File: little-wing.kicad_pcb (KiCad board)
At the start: 2 copper layers, 116.9 x 94.5 mm, 72 parts, among them IC1 AP7335-WG-7, J1 nice!view, J2 Battery, J3 trackball, J4 trackball, SW1 Power, SW2 Reset, U1 nice!nano v2, U2 PMW3610

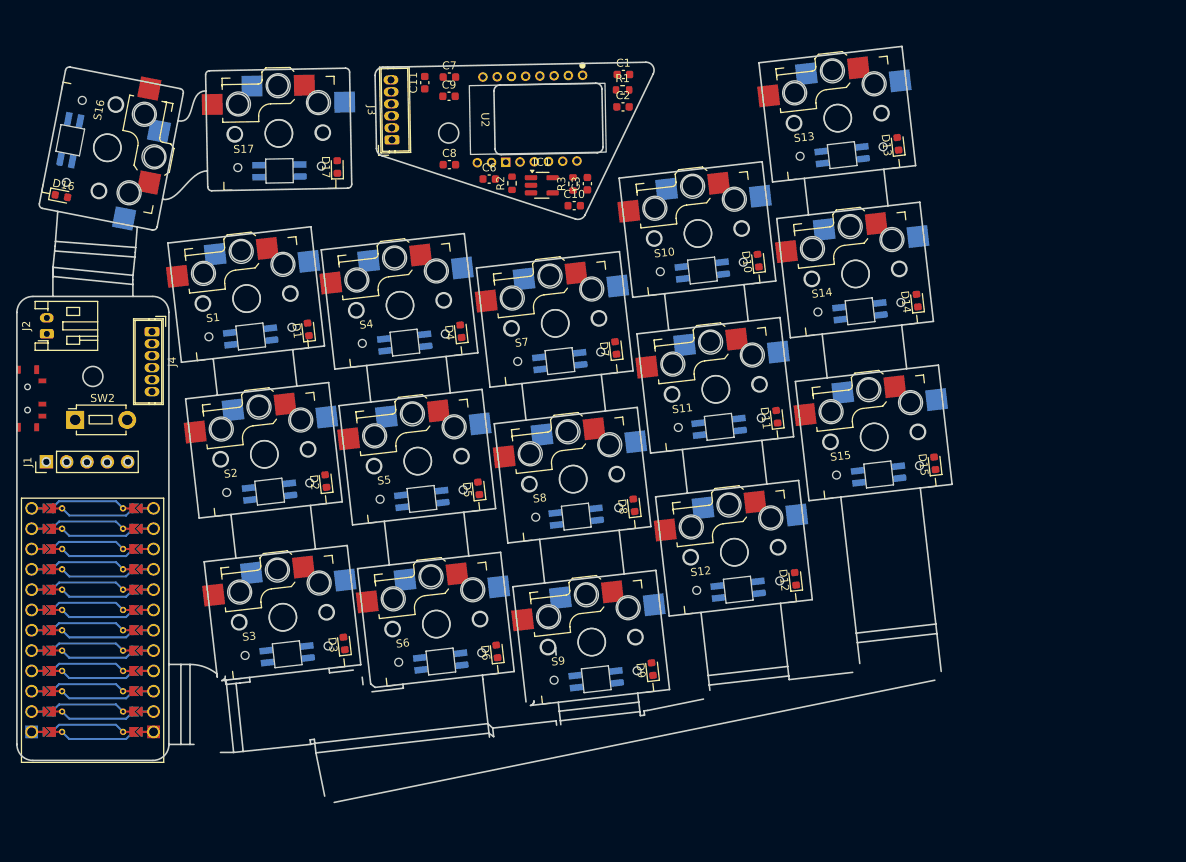
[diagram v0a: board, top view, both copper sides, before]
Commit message: Flipping the components in place
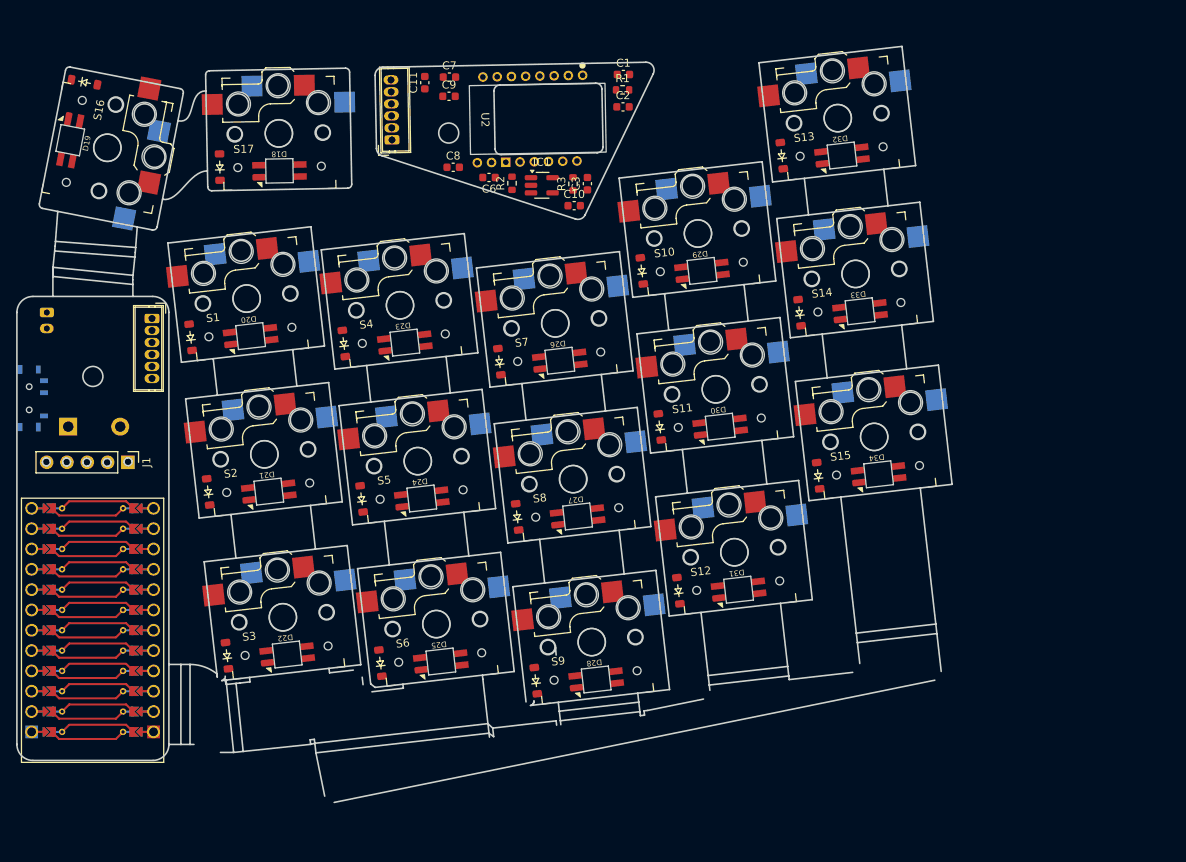
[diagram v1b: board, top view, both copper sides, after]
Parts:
- D1, D10, D11, D12, D13, D14, D15, D16, D17, D2, D3, D4, D5, D6, D7, D8, D9: footprint Diode_SMD:D_0603_1608Metric -> ScottoKeebs_Components:Diode_SOD-123
- D18, D19, D20, D21, D22, D23, D24, D25, D26, D27, D28, D29, D30, D31, D32, D33, D34, J2, SW1, SW2, U1: moved to B.Cu
- moved D14 14.8 mm to (164.7, 85.8)
- moved D2 14.8 mm to (90.8, 108.2)
- moved D1 14.7 mm to (88.6, 88.9)
- moved D3 14.7 mm to (93.2, 128.7)
- moved D4 14.7 mm to (107.8, 89.7)
- moved D12 14.7 mm to (149.6, 120.6)
- moved D5 14.7 mm to (110.0, 109.1)
- moved D11 14.7 mm to (147.2, 100.1)
- moved D17 14.7 mm to (92.2, 67.7)
- moved D8 14.7 mm to (129.4, 111.4)
- moved D15 14.7 mm to (167.1, 106.2)
- moved D7 14.6 mm to (127.2, 92.0)
- moved D6 14.6 mm to (112.3, 129.7)
- moved D9 14.6 mm to (131.8, 131.8)
- moved D10 14.6 mm to (145.0, 80.6)
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
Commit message: Remaking the PCB for better alignment
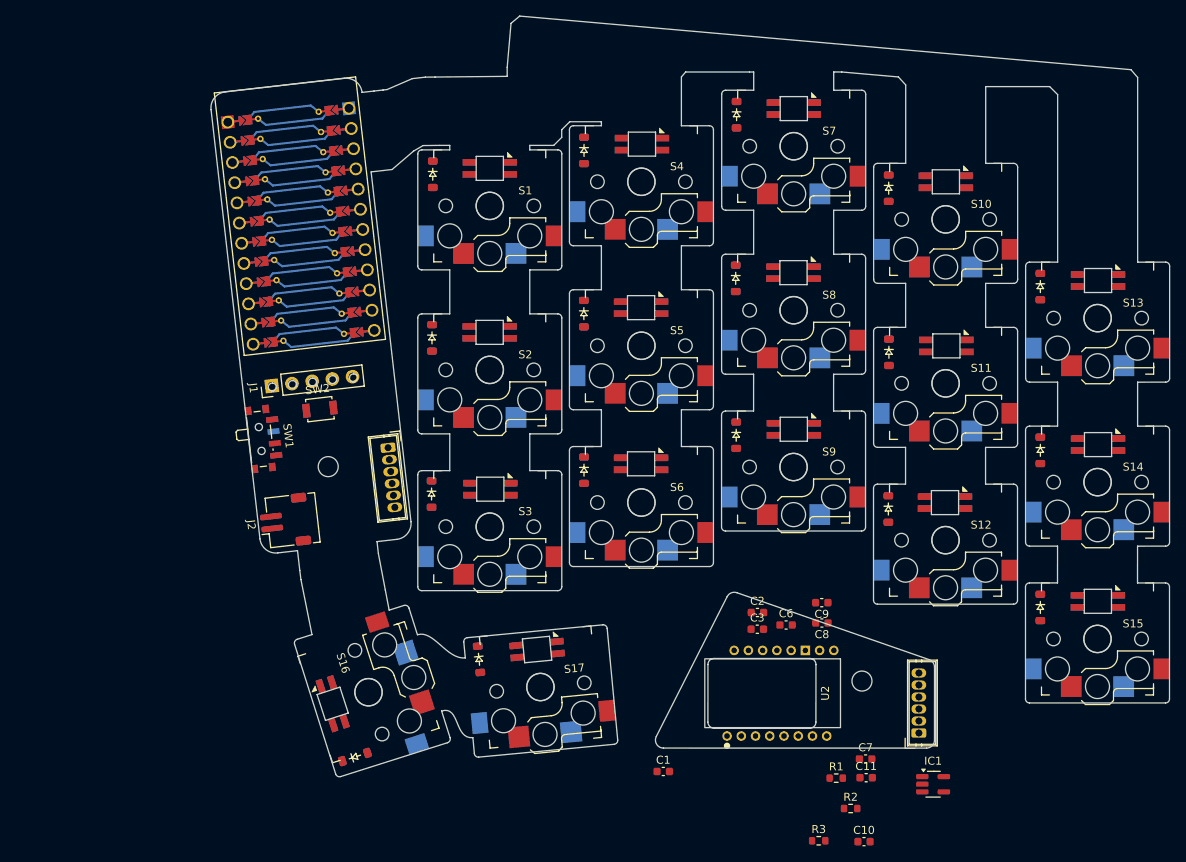
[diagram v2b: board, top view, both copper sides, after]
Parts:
- D1, D10, D11, D12, D13, D14, D15, D16, D17, D2, D3, D4, D5, D6, D7, D8, D9: footprint ScottoKeebs_Components:Diode_SOD-123 -> ScottoKeebs_Components:Diode_SOD-123_Reversible
- D18, D19, D20, D21, D22, D23, D24, D25, D26, D27, D28, D29, D30, D31, D32, D33, D34: footprint ScottoKeebs_Components:LED_SK6812MINI -> ScottoKeebs_Components:LED_SK6812MINI_Reversible; moved to F.Cu
- J2: footprint Connector_JST:JST_PH_S2B-PH-K_1x02_P2.00mm_Horizontal -> Connector_JST:JST_ZH_S2B-ZR-SM4A-TF_1x02-1MP_P1.50mm_Horizontal_Reversible; moved to F.Cu
- S1, S10, S11, S12, S13, S14, S15, S16, S17, S2, S3, S4, S5, S6, S7, S8, S9: footprint keyswitches:Kailh_socket_PG1350_reversible -> keyswitches:Kailh_socket_PG1350_reversible_better
- SW1: footprint switch:switch-MSK-12C02-smd -> Button_Switch_SMD:SW_SPDT_PCM12_Reversible; moved to F.Cu
- SW2: footprint ScottoKeebs_Components:Button_MJTP1243 -> Button_Switch_SMD:SW_SPST_B3U-1000P_Reversible; moved to F.Cu
- U1: moved to F.Cu
- moved D22 111.6 mm to (202.0, 81.8), turned to 0 degrees
- moved D20 111.0 mm to (202.0, 121.9), turned to 0 degrees
- moved D21 103.8 mm to (202.0, 102.3), turned to 0 degrees
- moved C11 102.9 mm to (173.0, 144.0), turned to 0 degrees
- moved C7 99.9 mm to (173.0, 141.6)
- moved J3 99.2 mm to (179.6, 138.4), turned to 90 degrees
- moved D16 90.9 mm to (109.1, 141.4), turned to 18 degrees
- moved R1 90.1 mm to (169.3, 144.0)
- moved IC1 89.4 mm to (181.4, 144.8)
- moved R2 88.9 mm to (171.1, 147.8), turned to 0 degrees
- moved R3 87.7 mm to (167.1, 151.9), turned to 0 degrees
- moved C10 87.4 mm to (172.8, 152.0)
- moved C1 87.3 mm to (147.7, 143.2)
- moved D25 87.1 mm to (183.0, 69.5), turned to 0 degrees
- moved C9 78.6 mm to (167.5, 122.1), turned to 180 degrees
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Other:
- board size 116.9 x 94.5 mm -> 119.8 x 95.1 mm

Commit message: Stashing the work before extending the cutouts
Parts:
- moved D29 0.14 mm to (144.9, 104.9)
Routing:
- net Col 0: track 0.00 -> 74.0 mm, vias 0 -> 3
- net Col 2: track 0.00 -> 73.8 mm, vias 0 -> 3
- net Col 4: track 0.00 -> 73.7 mm, vias 0 -> 3
- net Row 1: track 0.00 -> 73.1 mm, vias 0 -> 6
- net Col 1: track 0.00 -> 73.0 mm, vias 0 -> 3
- net Col 3: track 0.00 -> 73.0 mm, vias 0 -> 3
- net Row 0: track 0.00 -> 28.9 mm, vias 0 -> 6
- net Net-(D16-A): track 0.00 -> 28.5 mm, vias 0 -> 2
- net Net-(D17-A): track 0.00 -> 27.0 mm, vias 0 -> 2
- net Net-(D12-A): track 0.00 -> 26.9 mm, vias 0 -> 2
- net Net-(D13-A): track 0.00 -> 26.8 mm, vias 0 -> 2
- net Net-(D14-A): track 0.00 -> 26.4 mm, vias 0 -> 2
- net Net-(D5-A): track 0.00 -> 26.4 mm, vias 0 -> 2
- net Net-(D11-A): track 0.00 -> 26.4 mm, vias 0 -> 2
- net Net-(D1-A): track 0.00 -> 26.4 mm, vias 0 -> 2
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
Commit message: Making a column work
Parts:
- D1, D10, D11, D12, D13, D14, D15, D16, D17, D2, D3, D4, D5, D6, D7, D8, D9: moved to B.Cu
- moved D20 93.3 mm to (126.0, 67.8)
- moved D33 83.5 mm to (202.0, 102.3)
- moved D22 80.4 mm to (126.0, 107.9)
- moved D21 77.3 mm to (126.0, 88.3)
- moved D32 76.3 mm to (202.0, 81.8)
- moved D34 67.8 mm to (202.0, 121.9)
- moved D23 58.7 mm to (145.0, 64.8)
- moved D31 56.9 mm to (182.9, 109.6)
- moved D29 52.0 mm to (183.0, 69.5)
- moved D25 52.0 mm to (144.9, 104.9)
- moved D30 45.5 mm to (182.9, 90.0)
- moved D28 40.1 mm to (164.1, 100.5)
- moved D26 40.1 mm to (164.0, 60.4)
- moved D24 38.5 mm to (144.9, 85.3)
- moved C2 3.44 mm to (156.0, 123.8), turned to 180 degrees
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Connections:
- D18 pad 1: unconnected-(D18-DOUT-Pad1) -> VCC
- D18 pad 2: GND -> unconnected-(D18-DOUT-Pad2)
- D18 pad 3: Net-(D18-DIN) -> GND
- D18 pad 4: VCC -> Net-(D18-DIN)
- D19 pad 1: Net-(D18-DIN) -> VCC
- D19 pad 2: GND -> Net-(D18-DIN)
- D19 pad 3: Net-(D19-DIN) -> GND
- D19 pad 4: VCC -> Net-(D19-DIN)
- D20 pad 1: Net-(D19-DIN) -> VCC
- D20 pad 2: GND -> Net-(D19-DIN)
- D20 pad 3: Net-(D20-DIN) -> GND
- D20 pad 4: VCC -> Net-(D20-DIN)
- D21 pad 1: Net-(D20-DIN) -> VCC
- D21 pad 2: GND -> Net-(D20-DIN)
- D21 pad 3: Net-(D21-DIN) -> GND
- D21 pad 4: VCC -> Net-(D21-DIN)
- D22 pad 1: Net-(D21-DIN) -> VCC
- D22 pad 2: GND -> Net-(D21-DIN)
- D22 pad 3: Net-(D22-DIN) -> GND
- D22 pad 4: VCC -> Net-(D22-VDD)
- D23 pad 1: Net-(D22-DIN) -> VCC
- D23 pad 2: GND -> Net-(D22-VDD)
- D23 pad 3: Net-(D23-DIN) -> GND
- D23 pad 4: VCC -> Net-(D23-DIN)
- D24 pad 1: Net-(D23-DIN) -> VCC
- D24 pad 2: GND -> Net-(D23-DIN)
- D24 pad 3: Net-(D24-DIN) -> GND
- D24 pad 4: VCC -> Net-(D24-DIN)
- D25 pad 1: Net-(D24-DIN) -> VCC
- D25 pad 2: GND -> Net-(D24-DIN)
- D25 pad 3: Net-(D25-DIN) -> GND
- D25 pad 4: VCC -> Net-(D25-DIN)
- D26 pad 1: Net-(D25-DIN) -> VCC
- D26 pad 2: GND -> Net-(D25-DIN)
- D26 pad 3: Net-(D26-DIN) -> GND
- D26 pad 4: VCC -> Net-(D26-DIN)
- D27 pad 1: Net-(D26-DIN) -> VCC
- D27 pad 2: GND -> Net-(D26-DIN)
- D27 pad 3: Net-(D27-DIN) -> GND
- D27 pad 4: VCC -> Net-(D27-DIN)
- D28 pad 1: Net-(D27-DIN) -> VCC
- D28 pad 2: GND -> Net-(D27-DIN)
- D28 pad 3: Net-(D28-DIN) -> GND
- D28 pad 4: VCC -> Net-(D28-VDD)
- D29 pad 1: Net-(D28-DIN) -> VCC
- D29 pad 2: GND -> Net-(D28-VDD)
- D29 pad 3: Net-(D29-DIN) -> GND
- D29 pad 4: VCC -> Net-(D29-DIN)
- D30 pad 1: Net-(D29-DIN) -> VCC
- D30 pad 2: GND -> Net-(D29-DIN)
- D30 pad 3: Net-(D30-DIN) -> GND
- D30 pad 4: VCC -> Net-(D30-DIN)
- D31 pad 1: Net-(D30-DIN) -> VCC
- D31 pad 2: GND -> Net-(D30-DIN)
- D31 pad 3: Net-(D31-DIN) -> GND
- D31 pad 4: VCC -> Net-(D31-DIN)
- D32 pad 1: Net-(D31-DIN) -> VCC
- D32 pad 2: GND -> Net-(D31-DIN)
- D32 pad 3: Net-(D32-DIN) -> GND
- D32 pad 4: VCC -> Net-(D32-DIN)
- D33 pad 1: Net-(D32-DIN) -> VCC
- D33 pad 2: GND -> Net-(D32-DIN)
- D33 pad 3: Net-(D33-DIN) -> GND
- D33 pad 4: VCC -> Net-(D33-VDD)
- D34 pad 1: Net-(D33-DIN) -> VCC
- D34 pad 2: GND -> Net-(D33-VDD)
- D34 pad 3: RGB -> GND
- D34 pad 4: VCC -> RGB
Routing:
- net GND: track 0.00 -> 291.4 mm, vias 0 -> 15
- net VCC: track 0.00 -> 276.9 mm, vias 0 -> 17
- net Row 2: track 13.5 -> 194.6 mm, vias 5 -> 8
- net RGB: track 0.00 -> 82.6 mm, vias 0 -> 1
- net Net-(D32-DIN): track 0.00 -> 74.3 mm, vias 0 -> 2
- net Net-(D25-DIN): track 0.00 -> 70.7 mm, vias 0 -> 2
- net Net-(D22-VDD): track 0.00 -> 69.3 mm, vias 0 -> 2
- net Col 4: track 73.7 -> 124.4 mm
- net Row 1: track 73.1 -> 123.7 mm
- net Net-(D31-DIN): track 0.00 -> 46.9 mm, vias 0 -> 2
- net Net-(D23-DIN): track 0.00 -> 45.7 mm, vias 0 -> 2
- net Net-(D20-DIN): track 0.00 -> 45.4 mm, vias 0 -> 2
- net Net-(D24-DIN): track 0.00 -> 45.3 mm, vias 0 -> 2
- net Net-(D21-DIN): track 0.00 -> 44.7 mm, vias 0 -> 2
- net Net-(D33-VDD): track 0.00 -> 42.5 mm, vias 0 -> 2
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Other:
- outline, holes or cut-outs redrawn

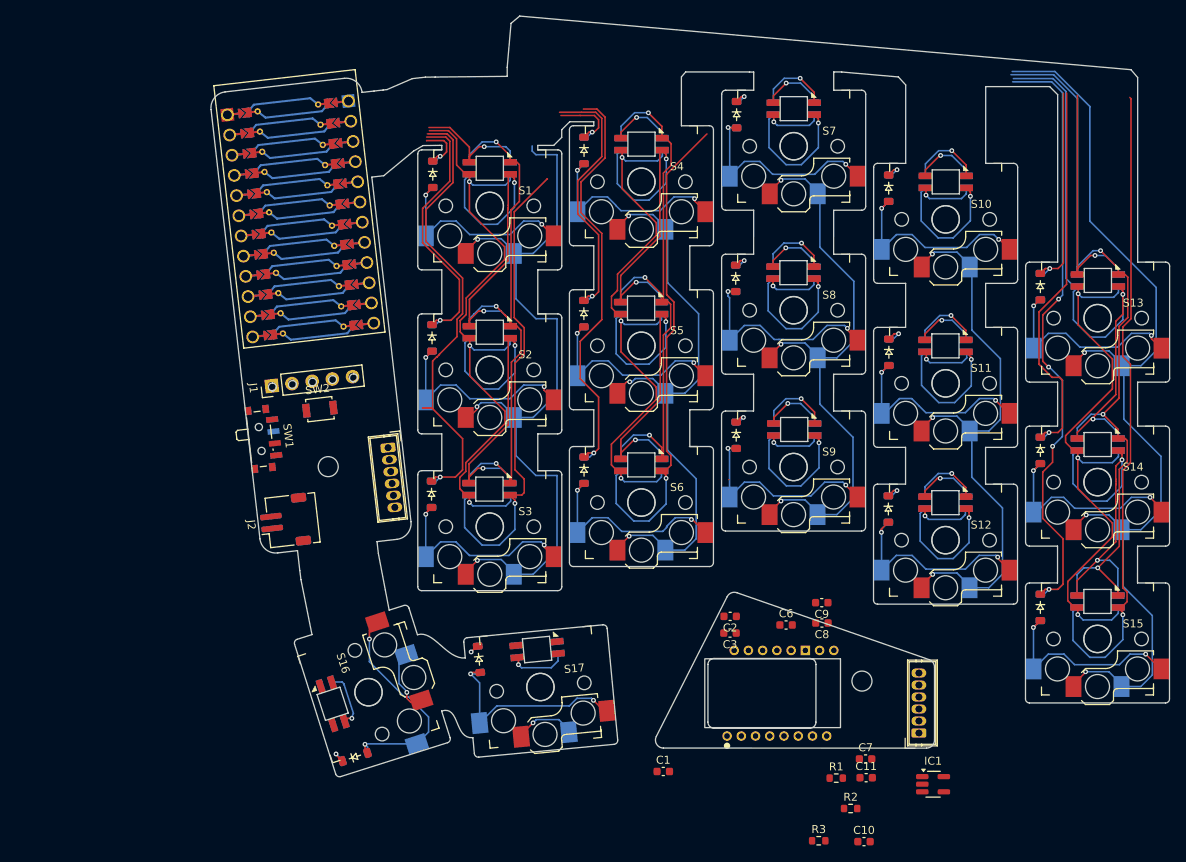
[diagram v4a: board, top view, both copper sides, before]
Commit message: Sorting out the main reversible pads
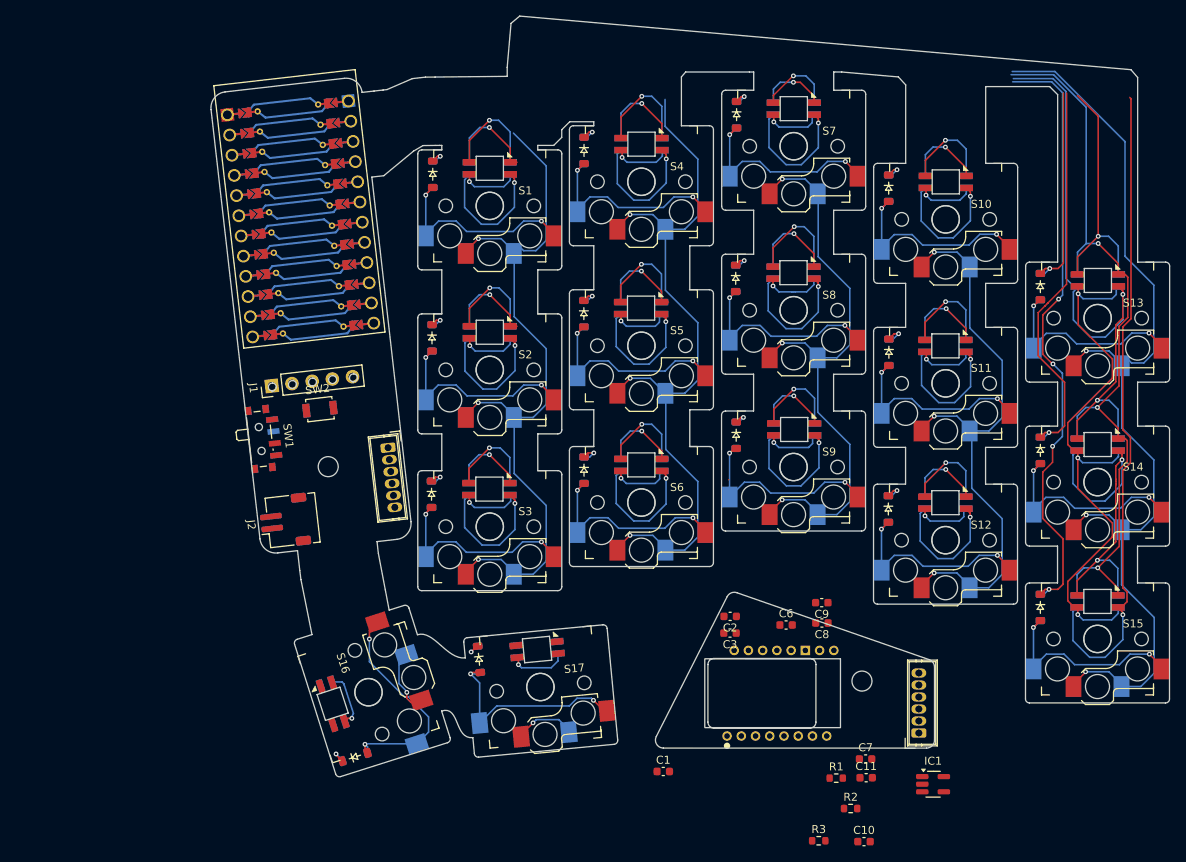
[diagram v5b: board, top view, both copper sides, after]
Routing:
- net Row 2: track 194.6 -> 87.9 mm
- net VCC: track 276.9 -> 175.8 mm
- net GND: track 291.4 -> 226.6 mm
- net Row 1: track 123.7 -> 62.4 mm
- net Net-(D25-DIN): track 70.7 -> 26.9 mm
- net Net-(D22-VDD): track 69.3 -> 30.2 mm
- net Col 1: track 73.0 -> 94.2 mm
- net Net-(D24-DIN): track 45.3 -> 28.4 mm
- net Net-(D23-DIN): track 45.7 -> 29.3 mm
- net Net-(D20-DIN): track 45.4 -> 29.4 mm
- net Net-(D21-DIN): track 44.7 -> 28.8 mm
- net Row 0: track 50.2 -> 39.0 mm
- net Net-(D26-DIN): track 24.5 -> 29.5 mm
- net Col 0: track 98.6 -> 93.7 mm
- net Net-(D29-DIN): track 24.6 -> 29.1 mm
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
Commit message: Connecting the reversible pads together
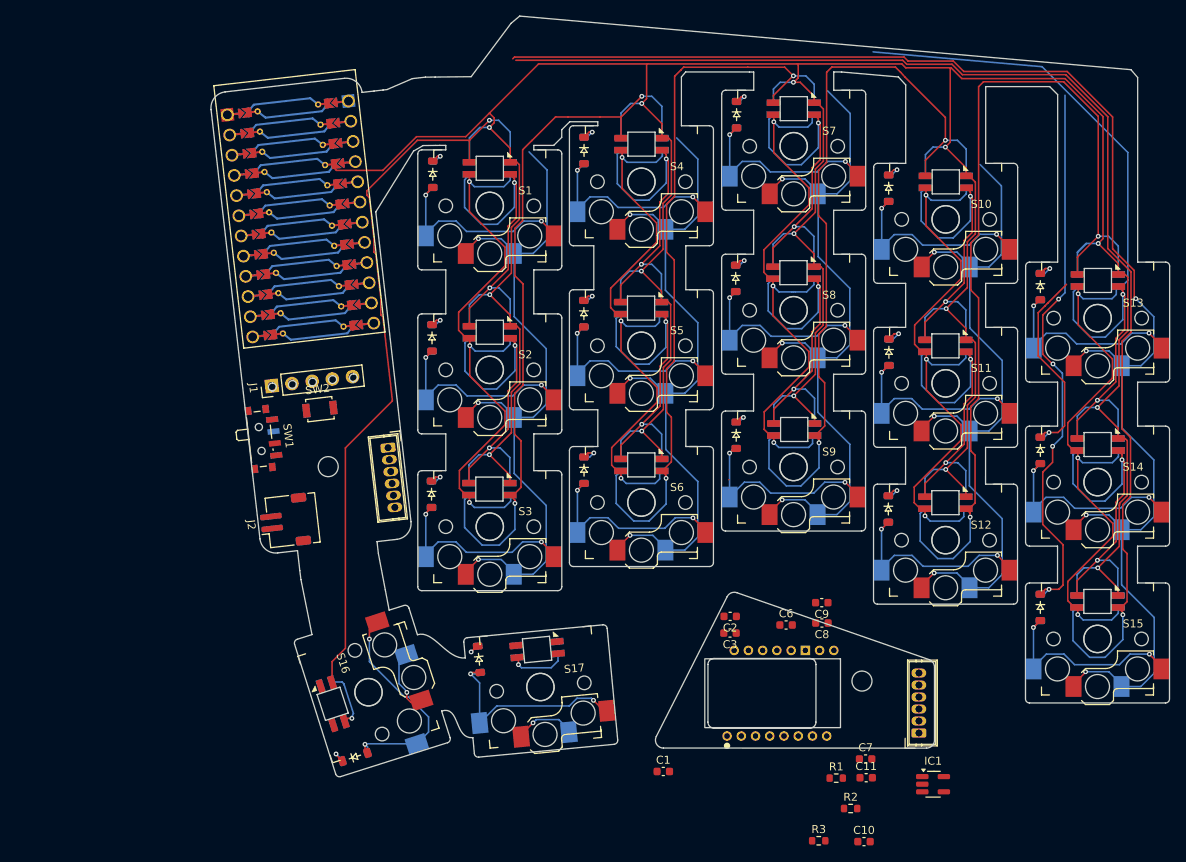
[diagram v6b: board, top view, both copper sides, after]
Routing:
- net GND: track 226.6 -> 489.1 mm
- net VCC: track 175.8 -> 421.0 mm
- net Net-(D19-DIN): track 13.3 -> 93.8 mm
- net RGB: track 82.6 -> 158.4 mm
- net Net-(D31-DIN): track 47.8 -> 116.0 mm
- net Net-(D28-VDD): track 28.6 -> 96.7 mm
- net Net-(D25-DIN): track 26.9 -> 94.0 mm
- net Col 4: track 124.0 -> 188.9 mm, vias 3 -> 4
- net Net-(D22-VDD): track 30.2 -> 89.8 mm
- net Net-(D32-DIN): track 76.3 -> 44.5 mm
- net Row 1: track 62.4 -> 38.5 mm
- net Row 0: track 39.0 -> 15.7 mm
- net Col 2: track 73.3 -> 90.5 mm
- net Col 3: track 73.2 -> 90.3 mm
- net Net-(D29-DIN): track 29.1 -> 44.2 mm
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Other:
- outline, holes or cut-outs redrawn

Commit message: Saving the main lanes progress
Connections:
- S1 pad 1: Col 0 -> Col 4
- S10 pad 1: Col 3 -> Col 1
- S11 pad 1: Col 3 -> Col 1
- S12 pad 1: Col 3 -> Col 1
- S13 pad 1: Col 4 -> Col 0
- S14 pad 1: Col 4 -> Col 0
- S15 pad 1: Col 4 -> Col 0
- S2 pad 1: Col 0 -> Col 4
- S3 pad 1: Col 0 -> Col 4
- S4 pad 1: Col 1 -> Col 3
- S5 pad 1: Col 1 -> Col 3
- S6 pad 1: Col 1 -> Col 3
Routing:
- net Row 2: track 81.0 -> 229.9 mm, vias 8 -> 16
- net Col 0: track 91.4 -> 209.9 mm
- net VCC: track 421.0 -> 535.6 mm, vias 17 -> 25
- net Col 1: track 88.8 -> 179.2 mm
- net Row 1: track 38.5 -> 125.1 mm, vias 6 -> 7
- net Col 4: track 188.9 -> 123.4 mm, vias 4 -> 3
- net Col 2: track 90.5 -> 154.2 mm
- net Col 3: track 90.3 -> 139.1 mm
- net Net-(D22-DIN): track 89.8 -> 114.3 mm
- net RGB: track 158.4 -> 180.4 mm
- net Net-(D19-DIN): track 93.8 -> 109.5 mm
- net GND: track 489.1 -> 504.3 mm
- net Net-(D25-DIN): track 94.0 -> 104.9 mm
- net Net-(D28-DIN): track 96.7 -> 107.2 mm
- net Net-(D31-DIN): track 116.0 -> 124.0 mm
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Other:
- outline, holes or cut-outs redrawn
